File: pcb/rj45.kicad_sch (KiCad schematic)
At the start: 6 parts, among them J13 RJ45_HC612601A-M893-A

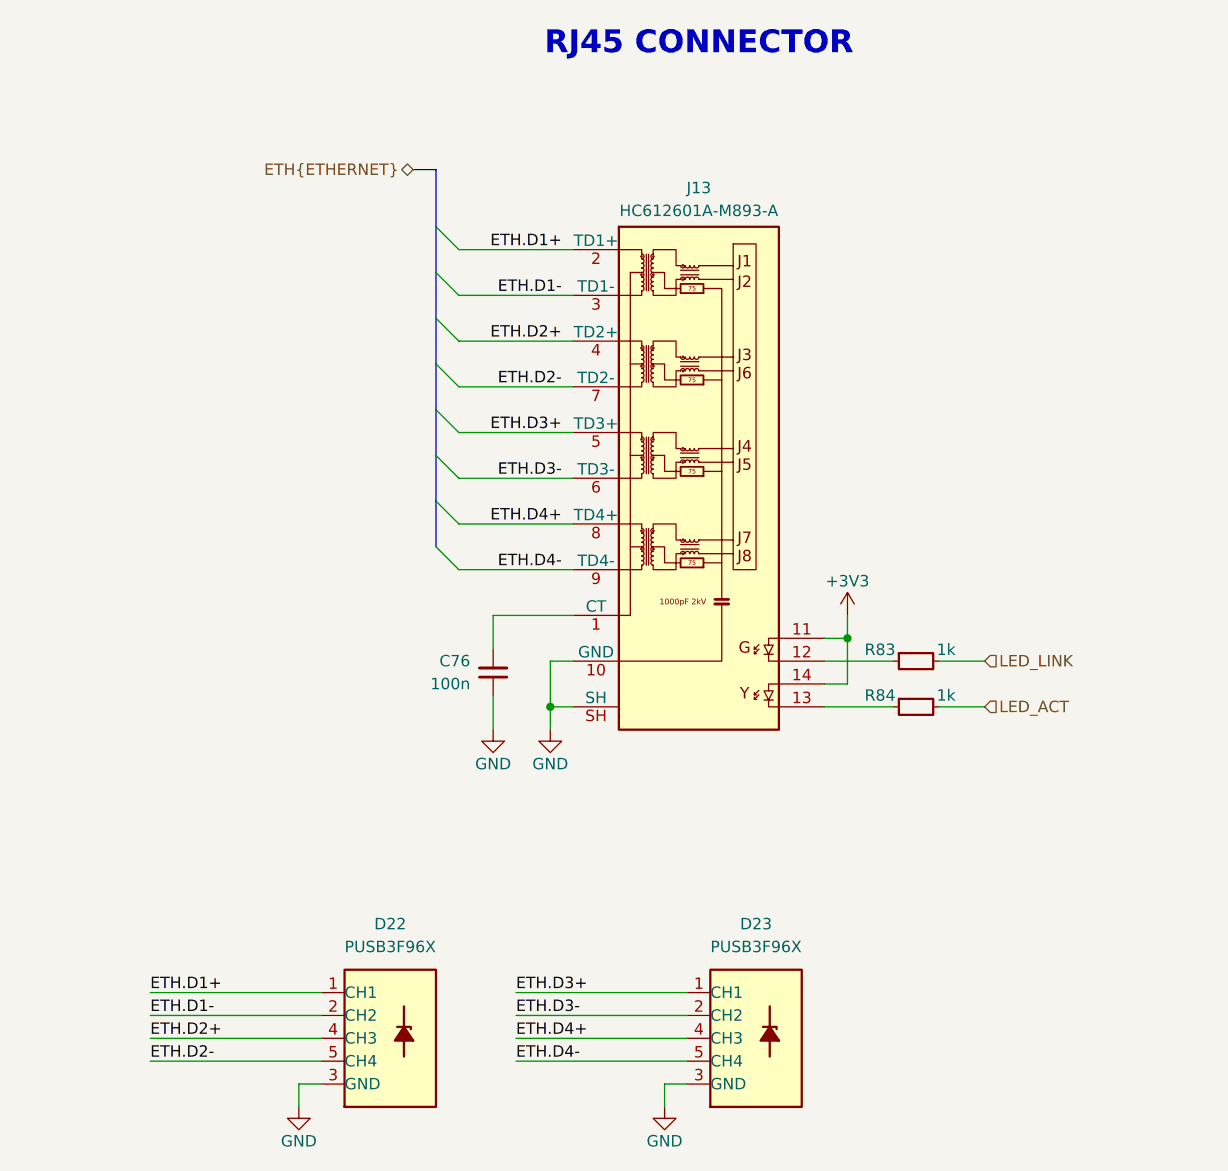
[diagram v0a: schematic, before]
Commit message: [#5] Refactor the schematic
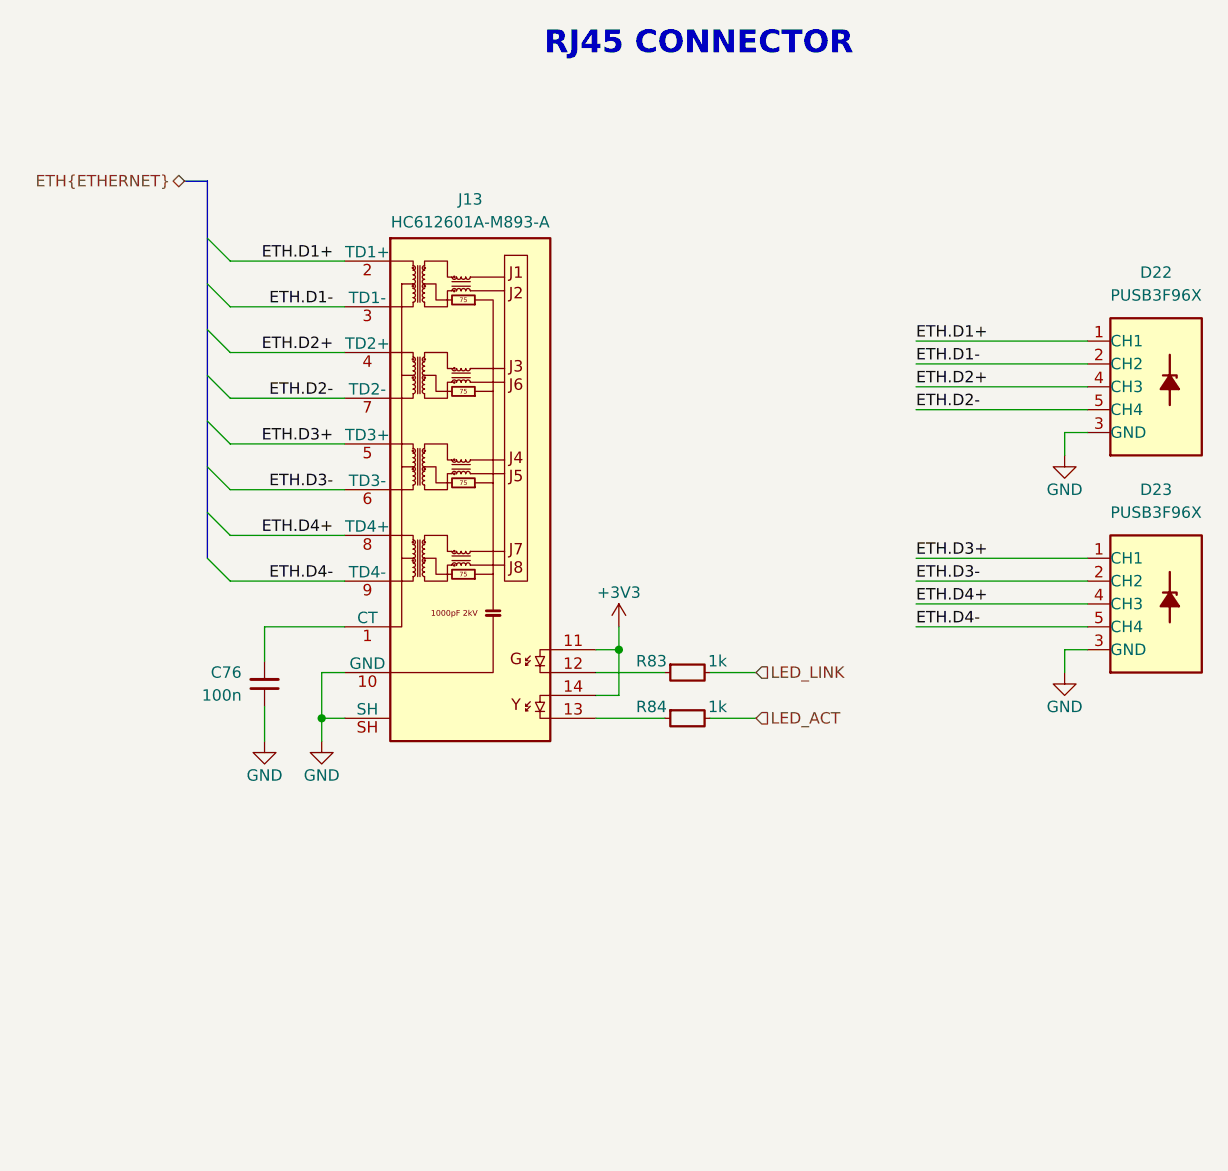
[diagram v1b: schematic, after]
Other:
- moved on the sheet: C76, D22, D23, J13, R83, R84
